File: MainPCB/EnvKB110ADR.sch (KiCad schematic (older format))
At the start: 238 parts, among them U1 XC6206PxxxMR, U2 STM32F411CEUx

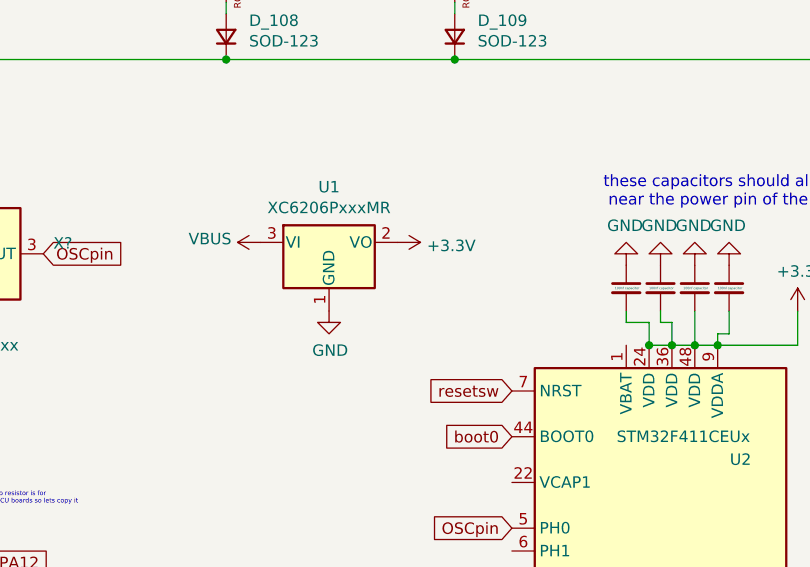
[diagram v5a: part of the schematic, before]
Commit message: added decoupling capacitors for LDO
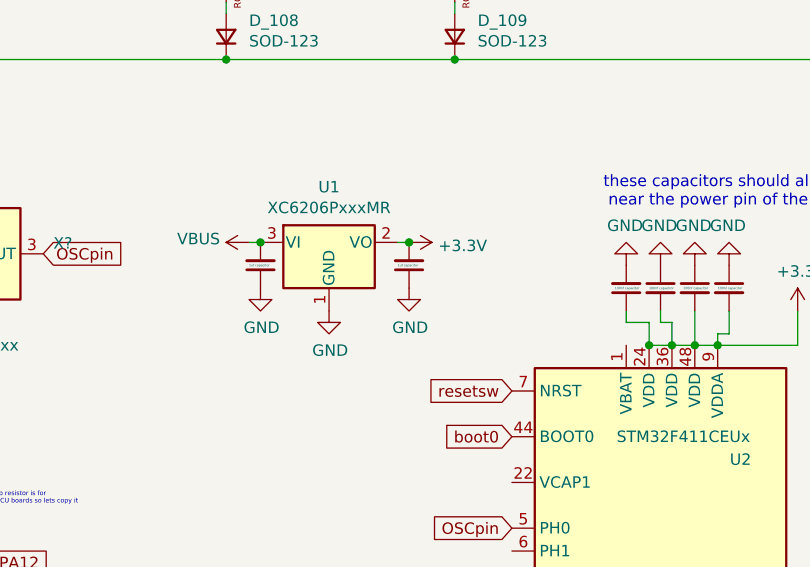
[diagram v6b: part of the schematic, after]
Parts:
- added C? (x2): 1uf capacitor, Capacitor_SMD:C_0402_1005Metric, symbol Device:C_Small
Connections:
- net +3V3: now also C1.1, C?.2; no longer C1.2
- net GND: now also C1.2, C?.1, C?.1; no longer C1.1
- net VBUS: now also C?.2
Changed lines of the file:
@@
 L power:+3.3V #PWR0104
 U 1 1 612BF658
-P 12200 9400
-F 0 "#PWR0104" H 12200 9250 50  0001 C CNN
-F 1 "+3.3V" V 12215 9528 50  0000 L CNN
-F 2 "" H 12200 9400 50  0001 C CNN
-F 3 "" H 12200 9400 50  0001 C CNN
-	1    12200 9400
+P 12250 9400
+F 0 "#PWR0104" H 12250 9250 50  0001 C CNN
+F 1 "+3.3V" V 12265 9528 50  0000 L CNN
+F 2 "" H 12250 9400 50  0001 C CNN
+F 3 "" H 12250 9400 50  0001 C CNN
+	1    12250 9400
 	0    1    1    0
 $EndComp
@@
 F 3 "~" H 13200 9600 50  0001 C CNN
 	1    13200 9600
-	1    0    0    -1
+	1    0    0    1
 $EndComp
 $Comp
@@
 L power:VBUS #PWR0115
 U 1 1 615E9702
-P 11600 9400
-F 0 "#PWR0115" H 11600 9250 50  0001 C CNN
-F 1 "VBUS" V 11615 9527 50  0000 L CNN
-F 2 "" H 11600 9400 50  0001 C CNN
-F 3 "" H 11600 9400 50  0001 C CNN
-	1    11600 9400
+P 11550 9400
+F 0 "#PWR0115" H 11550 9250 50  0001 C CNN
+F 1 "VBUS" V 11565 9527 50  0000 L CNN
+F 2 "" H 11550 9400 50  0001 C CNN
+F 3 "" H 11550 9400 50  0001 C CNN
+	1    11550 9400
 	0    -1   -1   0
 $EndComp
@@
 Wire Wire Line
 	7900 10600 7700 10600
+Wire Wire Line
+	11550 9400 11600 9400
+Wire Wire Line
+	12200 9400 12250 9400
+$Comp
+L Device:C_Small C?
+U 1 1 60F895E0
+P 12250 9500
+F 0 "C?" H 12342 9546 50  0001 L CNN
+F 1 "1uf capacitor" H 12200 9500 10  0000 L CNN
+F 2 "Capacitor_SMD:C_0402_1005Metric" H 12250 9500 50  0001 C CNN
+F 3 "~" H 12250 9500 50  0001 C CNN
+	1    12250 9500
+	1    0    0    1
+$EndComp
+Connection ~ 12250 9400
+$Comp
+L Device:C_Small C?
+U 1 1 60F8A0DF
+P 11600 9500
+F 0 "C?" H 11692 9546 50  0001 L CNN
+F 1 "1uf capacitor" H 11550 9500 10  0000 L CNN
+F 2 "Capacitor_SMD:C_0402_1005Metric" H 11600 9500 50  0001 C CNN
+F 3 "~" H 11600 9500 50  0001 C CNN
+	1    11600 9500
+	1    0    0    1
+$EndComp
+Connection ~ 11600 9400
+$Comp
+L power:GND #PWR?
+U 1 1 60F8A613
+P 11600 9600
+F 0 "#PWR?" H 11600 9350 50  0001 C CNN
+F 1 "GND" H 11605 9427 50  0000 C CNN
+F 2 "" H 11600 9600 50  0001 C CNN
+F 3 "" H 11600 9600 50  0001 C CNN
+	1    11600 9600
+	1    0    0    -1
+$EndComp
+$Comp
+L power:GND #PWR?
+U 1 1 60F8D702
+P 12250 9600
+F 0 "#PWR?" H 12250 9350 50  0001 C CNN
+F 1 "GND" H 12255 9427 50  0000 C CNN
+F 2 "" H 12250 9600 50  0001 C CNN
+F 3 "" H 12250 9600 50  0001 C CNN
+	1    12250 9600
+	1    0    0    -1
+$EndComp
 $EndSCHEMATC

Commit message: annotated parts + notes adjustment
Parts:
- gave numbers to parts that had none: 9
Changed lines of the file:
@@
 $EndComp
 $Comp
-L Oscillator:ECS-2520MV-xxx-xx X?
+L Oscillator:ECS-2520MV-xxx-xx X1
 U 1 1 60E5B405
 P 10250 9450
-F 0 "X?" H 10694 9496 50  0000 L CNN
-F 1 "ECS-2520MV-xxx-xx" H 9850 9050 50  0000 L CNN
+F 0 "X1" H 10400 9100 50  0000 L CNN
+F 1 "ECS-2520MV-xxx-xx" H 10400 9200 50  0000 L CNN
 F 2 "Oscillator:Oscillator_SMD_ECS_2520MV-xxx-xx-4Pin_2.5x2.0mm" H 10700 9100 50  0001 C CNN
 F 3 "https://www.ecsxtal.com/store/pdf/ECS-2520MV.pdf" H 10075 9575 50  0001 C CNN
@@
 OSCpin
 $Comp
-L power:+3.3V #PWR?
+L power:+3.3V #PWR01
 U 1 1 60E980B3
 P 10250 9150
-F 0 "#PWR?" H 10250 9000 50  0001 C CNN
+F 0 "#PWR01" H 10250 9000 50  0001 C CNN
 F 1 "+3.3V" H 10265 9323 50  0000 C CNN
 F 2 "" H 10250 9150 50  0001 C CNN
@@
 $EndComp
 $Comp
-L power:GND #PWR?
+L power:GND #PWR04
 U 1 1 60E99EB6
 P 10250 9750
-F 0 "#PWR?" H 10250 9500 50  0001 C CNN
+F 0 "#PWR04" H 10250 9500 50  0001 C CNN
 F 1 "GND" H 10255 9577 50  0000 C CNN
 F 2 "" H 10250 9750 50  0001 C CNN
@@
 boot0
 $Comp
-L power:GND #PWR?
+L power:GND #PWR07
 U 1 1 60E6F770
 P 8100 10100
-F 0 "#PWR?" H 8100 9850 50  0001 C CNN
+F 0 "#PWR07" H 8100 9850 50  0001 C CNN
 F 1 "GND" H 8105 9927 50  0000 C CNN
 F 2 "" H 8100 10100 50  0001 C CNN
@@
 $EndComp
 $Comp
-L power:GND #PWR?
+L power:GND #PWR06
 U 1 1 60E6FF51
 P 7800 10100
-F 0 "#PWR?" H 7800 9850 50  0001 C CNN
+F 0 "#PWR06" H 7800 9850 50  0001 C CNN
 F 1 "GND" H 7805 9927 50  0000 C CNN
 F 2 "" H 7800 10100 50  0001 C CNN
@@
 $EndComp
 $Comp
-L Device:R_Small R?
+L Device:R_Small R6
 U 1 1 60E71B24
 P 7800 10000
-F 0 "R?" H 7859 10046 50  0001 L CNN
+F 0 "R6" H 7859 10046 50  0001 L CNN
 F 1 "100k 0402" V 7850 9900 20  0000 L CNN
 F 2 "Resistor_SMD:R_0402_1005Metric" H 7800 10000 50  0001 C CNN
@@
 $EndComp
 $Comp
-L Device:C_Small C?
+L Device:C_Small C7
 U 1 1 60E73582
 P 8100 10000
-F 0 "C?" H 8192 10046 50  0001 L CNN
+F 0 "C7" H 8192 10046 50  0001 L CNN
 F 1 "100nf 0402" H 8100 9950 20  0000 L CNN
 F 2 "Capacitor_SMD:C_0402_1005Metric" H 8100 10000 50  0001 C CNN
@@
 Connection ~ 8100 9850
 $Comp
-L Switch:SW_Push SW?
+L Switch:SW_Push SW1
 U 1 1 60EE310E
 P 7600 9850
-F 0 "SW?" H 7600 10135 50  0000 C CNN
+F 0 "SW1" H 7600 10135 50  0000 C CNN
 F 1 "Boot Mode" H 7600 10044 50  0000 C CNN
 F 2 "Button_Switch_SMD:SW_DIP_SPSTx01_Slide_6.7x4.1mm_W6.73mm_P2.54mm_LowProfile_JPin" H 7600 10043 50  0001 C CNN
@@
 Connection ~ 7800 9850
 $Comp
-L power:+3.3V #PWR?
+L power:+3.3V #PWR05
 U 1 1 60EE5DF1
 P 7400 9850
-F 0 "#PWR?" H 7400 9700 50  0001 C CNN
+F 0 "#PWR05" H 7400 9700 50  0001 C CNN
 F 1 "+3.3V" V 7415 9978 50  0000 L CNN
 F 2 "" H 7400 9850 50  0001 C CNN
@@
 resetsw
 $Comp
-L power:GND #PWR?
+L power:GND #PWR010
 U 1 1 60EED52E
 P 8100 10850
-F 0 "#PWR?" H 8100 10600 50  0001 C CNN
+F 0 "#PWR010" H 8100 10600 50  0001 C CNN
 F 1 "GND" H 8105 10677 50  0000 C CNN
 F 2 "" H 8100 10850 50  0001 C CNN
@@
 $EndComp
 $Comp
-L power:GND #PWR?
+L power:GND #PWR09
 U 1 1 60EEEB39
 P 7500 10850
-F 0 "#PWR?" H 7500 10600 50  0001 C CNN
+F 0 "#PWR09" H 7500 10600 50  0001 C CNN
 F 1 "GND" H 7505 10677 50  0000 C CNN
 F 2 "" H 7500 10850 50  0001 C CNN
@@
 $EndComp
 $Comp
-L Device:C_Small C?
+L Device:C_Small C8
 U 1 1 60EEF344
 P 8100 10750
-F 0 "C?" H 8192 10796 50  0000 L CNN
+F 0 "C8" H 8192 10796 50  0000 L CNN
 F 1 "100nf 0402" H 8192 10705 50  0000 L CNN
 F 2 "Capacitor_SMD:C_0402_1005Metric" H 8100 10750 50  0001 C CNN
@@
 $EndComp
 $Comp
-L Device:R_Small R?
+L Device:R_Small R7
 U 1 1 60EF0D18
 P 7600 10600
-F 0 "R?" V 7500 10600 50  0000 C CNN
+F 0 "R7" V 7500 10600 50  0000 C CNN
 F 1 "10K 0402" V 7550 10600 20  0000 C CNN
 F 2 "Resistor_SMD:R_0402_1005Metric" H 7600 10600 50  0001 C CNN
@@
 $EndComp
 $Comp
-L power:+3.3V #PWR?
+L power:+3.3V #PWR08
 U 1 1 60EF228D
 P 7500 10600
-F 0 "#PWR?" H 7500 10450 50  0001 C CNN
+F 0 "#PWR08" H 7500 10450 50  0001 C CNN
 F 1 "+3.3V" V 7515 10728 50  0000 L CNN
 F 2 "" H 7500 10600 50  0001 C CNN
@@
 Connection ~ 8100 10600
 $Comp
-L Switch:SW_Push SW?
+L Switch:SW_Push SW2
 U 1 1 60F65F42
 P 7700 10850
-F 0 "SW?" H 7700 10750 50  0000 C CNN
+F 0 "SW2" H 7700 10750 50  0000 C CNN
 F 1 "Reset Switch" H 7700 10800 20  0000 C CNN
 F 2 "Button_Switch_SMD:SW_DIP_SPSTx01_Slide_6.7x4.1mm_W6.73mm_P2.54mm_LowProfile_JPin" H 7700 11043 50  0001 C CNN
@@
 	12200 9400 12250 9400
 $Comp
-L Device:C_Small C?
+L Device:C_Small C6
 U 1 1 60F895E0
 P 12250 9500
-F 0 "C?" H 12342 9546 50  0001 L CNN
+F 0 "C6" H 12342 9546 50  0001 L CNN
 F 1 "1uf capacitor" H 12200 9500 10  0000 L CNN
 F 2 "Capacitor_SMD:C_0402_1005Metric" H 12250 9500 50  0001 C CNN
@@
 Connection ~ 12250 9400
 $Comp
-L Device:C_Small C?
+L Device:C_Small C5
 U 1 1 60F8A0DF
 P 11600 9500
-F 0 "C?" H 11692 9546 50  0001 L CNN
+F 0 "C5" H 11692 9546 50  0001 L CNN
 F 1 "1uf capacitor" H 11550 9500 10  0000 L CNN
 F 2 "Capacitor_SMD:C_0402_1005Metric" H 11600 9500 50  0001 C CNN
@@
 Connection ~ 11600 9400
 $Comp
-L power:GND #PWR?
+L power:GND #PWR02
 U 1 1 60F8A613
 P 11600 9600
-F 0 "#PWR?" H 11600 9350 50  0001 C CNN
+F 0 "#PWR02" H 11600 9350 50  0001 C CNN
 F 1 "GND" H 11605 9427 50  0000 C CNN
 F 2 "" H 11600 9600 50  0001 C CNN
@@
 $EndComp
 $Comp
-L power:GND #PWR?
+L power:GND #PWR03
 U 1 1 60F8D702
 P 12250 9600
-F 0 "#PWR?" H 12250 9350 50  0001 C CNN
+F 0 "#PWR03" H 12250 9350 50  0001 C CNN
 F 1 "GND" H 12255 9427 50  0000 C CNN
 F 2 "" H 12250 9600 50  0001 C CNN

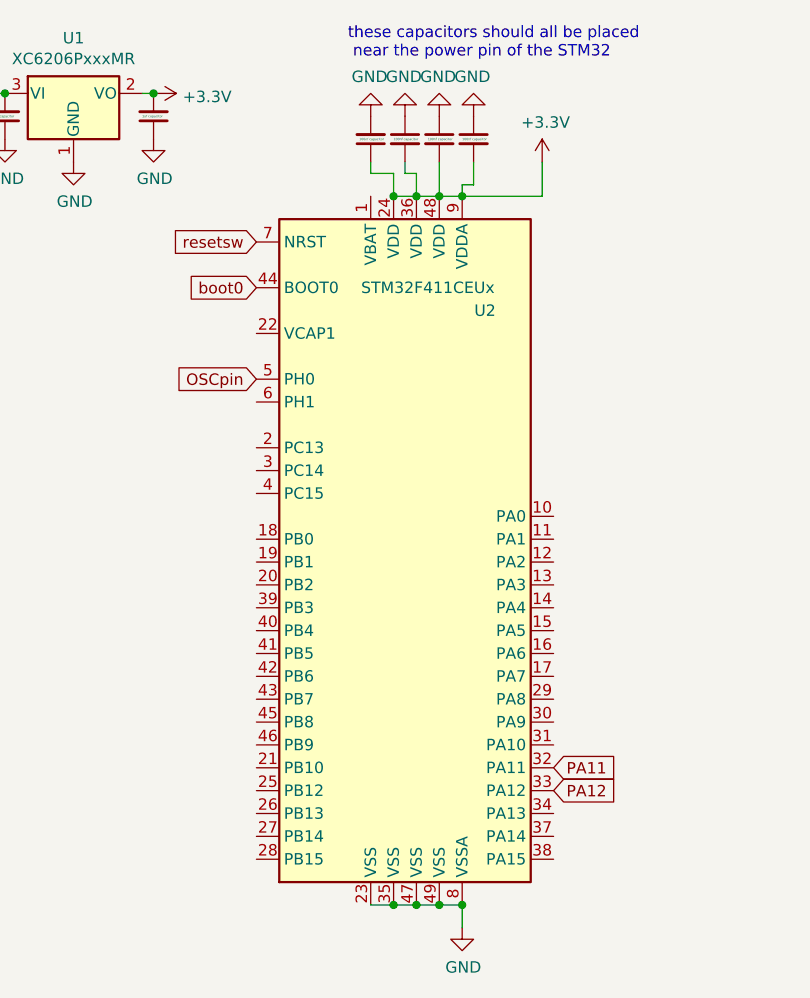
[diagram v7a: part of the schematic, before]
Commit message: Added row/col pins in the schematic for pcbnew to show them
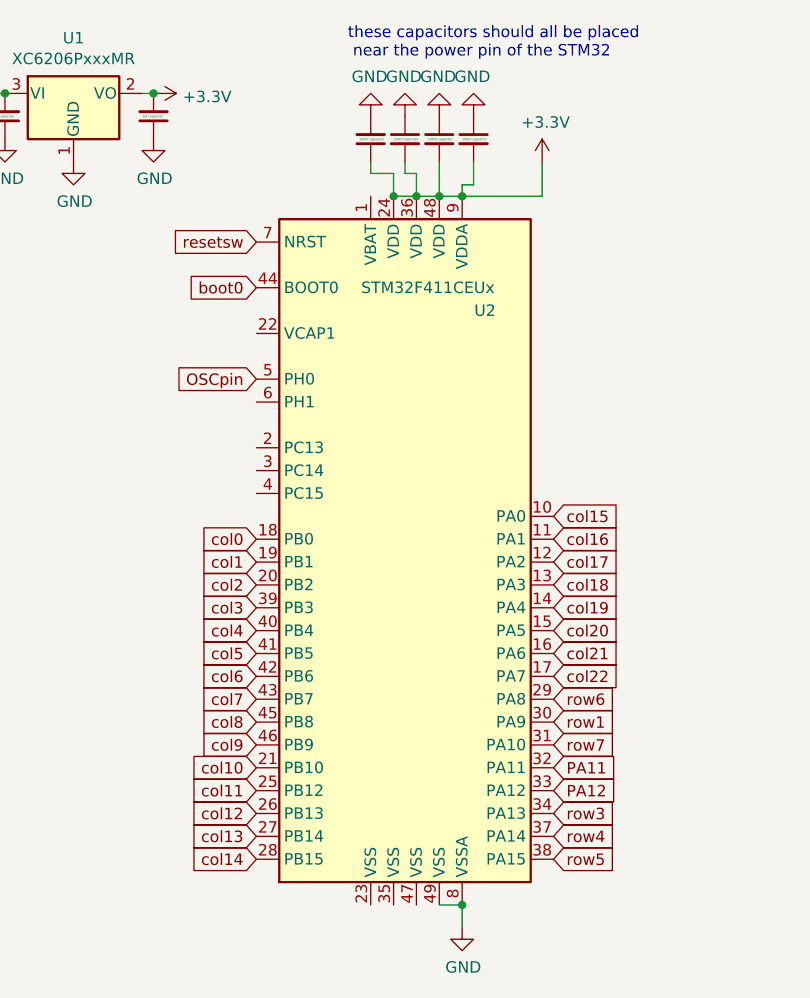
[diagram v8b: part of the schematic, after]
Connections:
- net GND: no longer U2.23 (VSS), U2.35 (VSS), U2.47 (VSS)
- net col0: now also U2.18 (PB0)
- net col1: now also U2.19 (PB1)
- net col10: now also U2.21 (PB10)
- net col11: now also U2.25 (PB12)
- net col12: now also U2.26 (PB13)
- net col13: now also U2.27 (PB14)
- net col14: now also U2.28 (PB15)
- net col15: now also U2.10 (PA0)
- net col16: now also U2.11 (PA1)
- net col17: now also U2.12 (PA2)
- net col19: now also U2.14 (PA4)
- net col2: now also U2.20 (PB2)
- net col20: now also U2.15 (PA5)
- net col21: now also U2.16 (PA6)
- net col22: now also U2.17 (PA7)
- net col3: now also U2.39 (PB3)
- net col4: now also U2.40 (PB4)
- net col5: now also U2.41 (PB5)
- net col6: now also U2.42 (PB6)
- net col7: now also U2.43 (PB7)
- net col8: now also U2.45 (PB8)
- net col9: now also U2.46 (PB9)
- net row1: now also U2.30 (PA9)
- net row3: now also U2.34 (PA13)
- net row4: now also U2.37 (PA14)
- net row5: now also U2.38 (PA15)
- net row6: now also U2.29 (PA8)
- net row7: now also U2.31 (PA10)
- net col18: now reaches U2.13 (PA3)
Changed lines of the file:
@@
 $EndComp
-Wire Wire Line
-	13200 12950 13300 12950
-Wire Wire Line
-	13400 12950 13300 12950
-Connection ~ 13300 12950
-Wire Wire Line
-	13400 12950 13500 12950
-Connection ~ 13400 12950
-Wire Wire Line
-	13500 12950 13600 12950
-Connection ~ 13500 12950
 Wire Wire Line
 	13600 13050 13600 12950
-Connection ~ 13600 12950
 $Comp
 L power:+3.3V #PWR0104
@@
 Wire Wire Line
 	13200 9750 13200 9700
-Connection ~ 13300 9850
 Wire Wire Line
 	13400 9850 13400 9750
@@
 Wire Wire Line
 	13350 9750 13350 9700
-Wire Wire Line
-	13500 9850 13500 9700
 Wire Wire Line
 	13600 9850 13600 9800
@@
 	1    0    0    -1
 $EndComp
+Text GLabel 12700 11350 0    50   Input ~ 0
+col0
+Text GLabel 12700 11450 0    50   Input ~ 0
+col1
+Text GLabel 12700 11550 0    50   Input ~ 0
+col2
+Text GLabel 12700 11650 0    50   Input ~ 0
+col3
+Text GLabel 12700 11750 0    50   Input ~ 0
+col4
+Text GLabel 12700 11850 0    50   Input ~ 0
+col5
+Text GLabel 12700 11950 0    50   Input ~ 0
+col6
+Text GLabel 12700 12050 0    50   Input ~ 0
+col7
+Text GLabel 12700 12150 0    50   Input ~ 0
+col8
+Text GLabel 12700 12250 0    50   Input ~ 0
+col9
+Text GLabel 12700 12350 0    50   Input ~ 0
+col10
+Text GLabel 12700 12450 0    50   Input ~ 0
+col11
+Text GLabel 12700 12550 0    50   Input ~ 0
+col12
+Text GLabel 12700 12650 0    50   Input ~ 0
+col13
+Text GLabel 12700 12750 0    50   Input ~ 0
+col14
+Text GLabel 14000 11250 2    50   Input ~ 0
+col15
+Text GLabel 14000 11350 2    50   Input ~ 0
+col16
+Text GLabel 14000 11450 2    50   Input ~ 0
+col17
+Text GLabel 14000 11550 2    50   Input ~ 0
+col18
+Text GLabel 14000 11650 2    50   Input ~ 0
+col19
+Text GLabel 14000 11750 2    50   Input ~ 0
+col20
+Text GLabel 14000 11850 2    50   Input ~ 0
+col21
+Text GLabel 14000 11950 2    50   Input ~ 0
+col22
+Text GLabel 14000 12150 2    50   Input ~ 0
+row1
+Text GLabel 14000 12550 2    50   Input ~ 0
+row3
+Text GLabel 14000 12650 2    50   Input ~ 0
+row4
+Text GLabel 14000 12750 2    50   Input ~ 0
+row5
+Text GLabel 14000 12050 2    50   Input ~ 0
+row6
+Text GLabel 14000 12250 2    50   Input ~ 0
+row7
+Wire Wire Line
+	13500 12950 13600 12950
+Wire Wire Line
+	13500 9700 13500 9850
+Connection ~ 13300 9850
+Connection ~ 13600 12950
 $EndSCHEMATC
